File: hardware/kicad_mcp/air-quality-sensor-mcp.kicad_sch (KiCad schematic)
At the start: 16 parts, among them J1 JST_PH_2pin_Battery, U1 XIAO_ESP32C3, U2 Adafruit_SCD41, U3 Adafruit_SGP41, U4 SSD1306_OLED_128x64, U5 TP4056_USB-C_Module

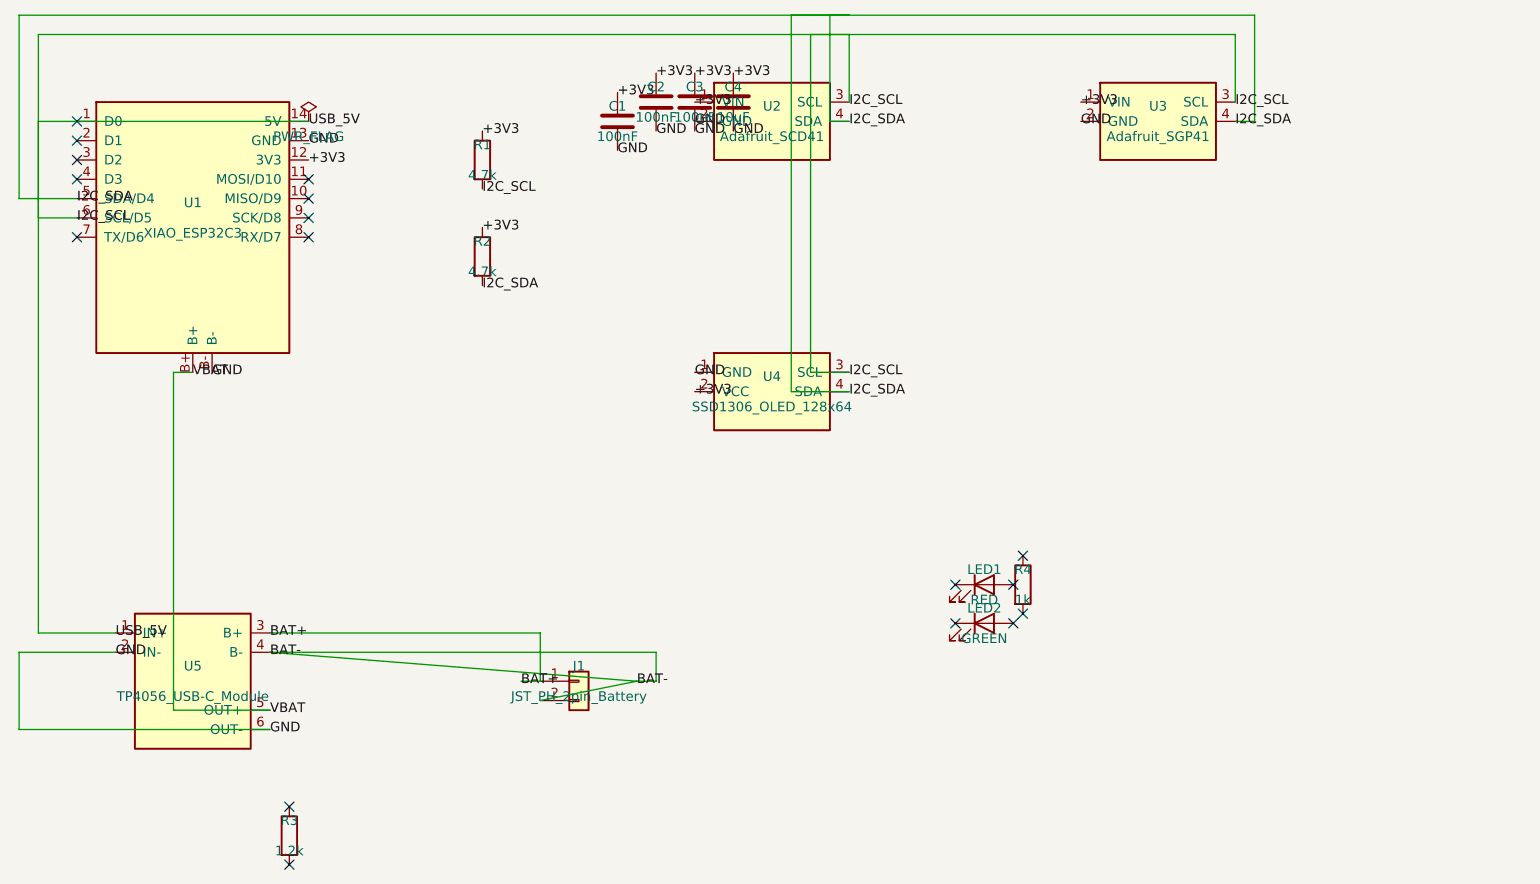
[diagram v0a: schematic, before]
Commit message: Finalize v3 MCP board respin: PMSA003I PM sensor + 5 V boost power tree
Commit the June 2026 design session that was never landed: U1 switched to a
through-hole DIP footprint, Adafruit PMSA003I (U6) added on the shared I2C
bus, TPS61023-class 5 V boost (U7) + SS14 Schottky (D1) power tree for
battery-only operation. 19 symbols, ERC 0 errors, 160 routed tracks, DRC
clean; manufacturing outputs regenerated. BOARD-DESIGN-NOTES.md records
board-specific status and open items; MCP-FUTURE-CHANGES.md records the
MCP-only workflow policy and validation baseline. Ignore local KiCad/MCP
editor artifacts (prl, validation caches, eval scratch files).
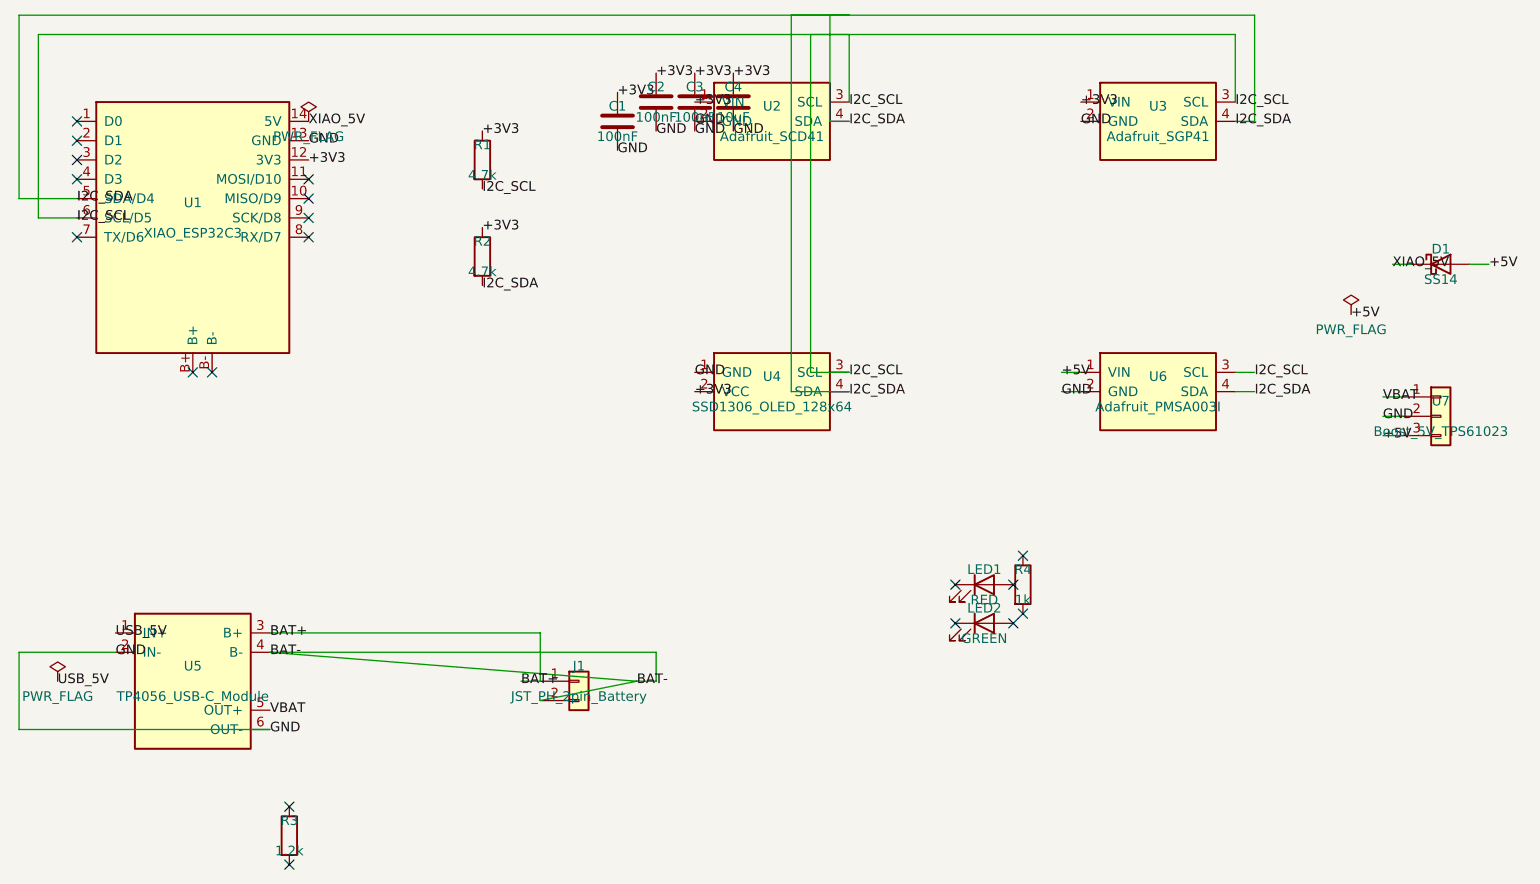
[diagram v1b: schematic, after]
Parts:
- added D1: SS14, Diode_SMD:D_SMA, symbol Device:D_Schottky
- added U6: Adafruit_PMSA003I, Connector_PinHeader_2.54mm:PinHeader_1x04_P2.54mm_Vertical, symbol AirQuality_Sensors:Adafruit_PMSA003I
- added U7: Boost_5V_TPS61023, Connector_PinHeader_2.54mm:PinHeader_1x03_P2.54mm_Vertical, symbol Connector_Generic:Conn_01x03
- U1: footprint AirQuality:XIAO_ESP32C3 -> Seeed_XIAO:XIAO-ESP32C3-DIP
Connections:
- net GND: now also U6.2 (GND), U7.2 (Pin_2); no longer U1.B-
- net I2C_SCL: now also U6.3 (SCL); no longer U1.14 (5V), U5.1 (IN+)
- net I2C_SDA: now also U6.4 (SDA)
- net VBAT: now also U7.1 (Pin_1); no longer U1.B+
- new net +5V: D1.2 (A), U6.1 (VIN), U7.3 (Pin_3)
- new net USB_5V: U5.1 (IN+)
- new net XIAO_5V: D1.1 (K), U1.14 (5V)
- no-connect marks 17 -> 19
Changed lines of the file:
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@@
     (rev "A")
+  )
+  (label "+5V" (at 203.2 101.6 0)
+    (effects (font (size 1.27 1.27)))
+  )
+  (symbol (lib_id "power:PWR_FLAG") (at 33.02 149.86 0.0) (unit 1)
+    (exclude_from_sim no) (in_bom yes) (on_board yes) (dnp no)
+    (property "Reference" "#PWR003" (at 33.02 147.86 0)
+      (effects (font (size 1.27 1.27)) (hide yes))
+    )
+    (property "Value" "PWR_FLAG" (at 33.02 151.86 0)
+      (effects (font (size 1.27 1.27)))
+    )
+    (instances
+      (project ""
+        (path "/025eedaf-9779-457c-a85c-2ea332d6b66a"
+          (reference "#PWR003") (unit 1)
+        )
+      )
+    )
+  )
+  (symbol (lib_id "power:PWR_FLAG") (at 203.2 101.6 0.0) (unit 1)
+    (exclude_from_sim no) (in_bom yes) (on_board yes) (dnp no)
+    (property "Reference" "#PWR002" (at 203.2 99.6 0)
+      (effects (font (size 1.27 1.27)) (hide yes))
+    )
+    (property "Value" "PWR_FLAG" (at 203.2 103.6 0)
+      (effects (font (size 1.27 1.27)))
+    )
+    (instances
+      (project ""
+        (path "/025eedaf-9779-457c-a85c-2ea332d6b66a"
+          (reference "#PWR002") (unit 1)
+        )
+      )
+    )
+  )
+  (wire (pts (xy 209.92 115.0) (xy 207.38 115.0))
+    (stroke (width 0) (type default))
+  )
+  (label "GND" (at 207.38 115.0 0)
+    (effects (font (size 1.27 1.27)))
+  )
+  (wire (pts (xy 209.92 112.46) (xy 207.38 112.46))
+    (stroke (width 0) (type default))
+  )
+  (label "VBAT" (at 207.38 112.46 0)
+    (effects (font (size 1.27 1.27)))
+  )
+  (wire (pts (xy 211.19 95.0) (xy 208.65 95.0))
+    (stroke (width 0) (type default))
+  )
+  (label "XIAO_5V" (at 208.65 95.0 0)
+    (effects (font (size 1.27 1.27)))
+  )
+  (wire (pts (xy 218.81 95.0) (xy 221.35 95.0))
+    (stroke (width 0) (type default))
+  )
+  (label "+5V" (at 221.35 95.0 0)
+    (effects (font (size 1.27 1.27)))
+  )
+  (wire (pts (xy 209.92 117.54) (xy 207.38 117.54))
+    (stroke (width 0) (type default))
+  )
+  (label "+5V" (at 207.38 117.54 0)
+    (effects (font (size 1.27 1.27)))
+  )
+  (symbol (lib_id "Connector_Generic:Conn_01x03") (at 215.0 115.0 0.0) (unit 1)
+    (exclude_from_sim no) (in_bom yes) (on_board yes) (dnp no)
+    (property "Reference" "U7" (at 215.0 113.0 0)
+      (effects (font (size 1.27 1.27)))
+    )
+    (property "Value" "Boost_5V_TPS61023" (at 215.0 117.0 0)
+      (effects (font (size 1.27 1.27)))
+    )
+    (property "Footprint" "Connector_PinHeader_2.54mm:PinHeader_1x03_P2.54mm_Vertical" (at 215.0 119.0 0)
+      (effects (font (size 1.27 1.27)) (hide yes))
+    )
+    (instances
+      (project ""
+        (path "/025eedaf-9779-457c-a85c-2ea332d6b66a"
+          (reference "U7") (unit 1)
+        )
+      )
+    )
+  )
+  (symbol (lib_id "Device:D_Schottky") (at 215.0 95.0 0.0) (unit 1)
+    (exclude_from_sim no) (in_bom yes) (on_board yes) (dnp no)
+    (property "Reference" "D1" (at 215.0 93.0 0)
+      (effects (font (size 1.27 1.27)))
+    )
+    (property "Value" "SS14" (at 215.0 97.0 0)
+      (effects (font (size 1.27 1.27)))
+    )
+    (property "Footprint" "Diode_SMD:D_SMA" (at 215.0 99.0 0)
+      (effects (font (size 1.27 1.27)) (hide yes))
+    )
+    (instances
+      (project ""
+        (path "/025eedaf-9779-457c-a85c-2ea332d6b66a"
+          (reference "D1") (unit 1)
+        )
+      )
+    )
+  )
+  (no_connect (at 53.34 109.22))
+  (no_connect (at 50.8 109.22))
+  (wire (pts (xy 187.96 111.76) (xy 190.5 111.76))
+    (stroke (width 0) (type default))
+  )
+  (label "I2C_SDA" (at 190.5 111.76 0)
+    (effects (font (size 1.27 1.27)))
+  )
+  (wire (pts (xy 187.96 109.22) (xy 190.5 109.22))
+    (stroke (width 0) (type default))
+  )
+  (label "I2C_SCL" (at 190.5 109.22 0)
+    (effects (font (size 1.27 1.27)))
+  )
+  (wire (pts (xy 167.64 111.76) (xy 165.1 111.76))
+    (stroke (width 0) (type default))
+  )
+  (label "GND" (at 165.1 111.76 0)
+    (effects (font (size 1.27 1.27)))
+  )
+  (wire (pts (xy 167.64 109.22) (xy 165.1 109.22))
+    (stroke (width 0) (type default))
+  )
+  (label "+5V" (at 165.1 109.22 0)
+    (effects (font (size 1.27 1.27)))
+  )
+  (symbol (lib_id "AirQuality_Sensors:Adafruit_PMSA003I") (at 177.8 111.76 0.0) (unit 1)
+    (exclude_from_sim no) (in_bom yes) (on_board yes) (dnp no)
+    (property "Reference" "U6" (at 177.8 109.76 0)
+      (effects (font (size 1.27 1.27)))
+    )
+    (property "Value" "Adafruit_PMSA003I" (at 177.8 113.76 0)
+      (effects (font (size 1.27 1.27)))
+    )
+    (property "Footprint" "Connector_PinHeader_2.54mm:PinHeader_1x04_P2.54mm_Vertical" (at 177.8 115.76 0)
+      (effects (font (size 1.27 1.27)) (hide yes))
+    )
+    (instances
+      (project ""
+        (path "/025eedaf-9779-457c-a85c-2ea332d6b66a"
+          (reference "U6") (unit 1)
+        )
+      )
+    )
+  )
+  (wire (pts (xy 96.52 152.4) (xy 109.22 149.86))
+    (stroke (width 0) (type default))
   )
   (wire (pts (xy 60.96 146.05) (xy 109.22 149.86))
@@
   (no_connect (at 35.56 76.2))
   (wire
-    (pts (xy 66.04 76.2) (xy 30.48 76.2))
-    (stroke (width 0) (type default))
-  )
-  (wire
-    (pts (xy 30.48 76.2) (xy 30.48 143.51))
-    (stroke (width 0) (type default))
-  )
-  (wire
-    (pts (xy 30.48 143.51) (xy 40.64 143.51))
-    (stroke (width 0) (type default))
-  )
-  (wire
-    (pts (xy 50.8 109.22) (xy 48.26 109.22))
-    (stroke (width 0) (type default))
-  )
-  (wire
-    (pts (xy 48.26 109.22) (xy 48.26 153.67))
-    (stroke (width 0) (type default))
-  )
-  (wire
-    (pts (xy 48.26 153.67) (xy 60.96 153.67))
-    (stroke (width 0) (type default))
-  )
-  (wire
     (pts (xy 60.96 143.51) (xy 96.52 143.51))
     (stroke (width 0) (type default))
@@
     (stroke (width 0) (type default))
   )
-  (label "VBAT" (at 50.8 109.22 0)
-    (effects (font (size 1.27 1.27)))
-  )
   (label "VBAT" (at 60.96 153.67 0)
     (effects (font (size 1.27 1.27)))
@@
     (effects (font (size 1.27 1.27)))
   )
-  (label "USB_5V" (at 66.04 76.2 0)
+  (label "XIAO_5V" (at 66.04 76.2 0)
     (effects (font (size 1.27 1.27)))
   )
@@
     (effects (font (size 1.27 1.27)))
   )
-  (label "GND" (at 53.34 109.22 0)
-    (effects (font (size 1.27 1.27)))
-  )
   (label "GND" (at 66.04 78.74 0)
     (effects (font (size 1.27 1.27)))
@@
       (effects (font (size 1.27 1.27)))
     )
-    (property "Footprint" "AirQuality:XIAO_ESP32C3" (at 50.8 92.9 0)
-      (effects (font (size 1.27 1.27)) hide)
-    )
+    (property "Footprint" "Seeed_XIAO:XIAO-ESP32C3-DIP" (at 50.8 92.9 0)
+      (effects (font (size 1.27 1.27)) hide)
+    )
